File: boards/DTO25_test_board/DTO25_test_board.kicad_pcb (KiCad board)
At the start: 2 copper layers, 55.2 x 57.8 mm, 9 parts, among them J1 MicroFit_11, J2 Ultrafit_4, J3 Ultrafit_2, J4 Ultrafit_4

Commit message: DTO@% test board MKII
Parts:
- removed J1: MicroFit_11, footprints:Molex_MicroFit_3.0-11x3.00mm_Angled
- removed J2, J4: Ultrafit_4, footprints:Ultrafit_4
- removed J3: Ultrafit_2, footprints:Ultrafit_2
- added P1: CONN_02X03, footprints:Pin_Header_Straight_2x03, F.Cu at (154.3, 108.6)
- added P2: CONN_02X03, footprints:Pin_Header_Straight_2x03, F.Cu at (188.0, 109.9)
- added R6: DTO25, footprints:DTO25, F.Cu at (202.6, 92.1)
- moved R5 75.4 mm to (191.1, 132.7)
- moved R4 61.7 mm to (179.7, 92.1), turned to 0 degrees
- moved R3 28.2 mm to (145.4, 92.1), turned to 0 degrees
- moved R2 27.1 mm to (156.8, 92.1), turned to 0 degrees
- moved R1 25.7 mm to (168.3, 92.1), turned to 0 degrees
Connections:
- R1 pad 1: /Thermal_Plane -> /ThermalPlane1
- R2 pad 1: /Thermal_Plane -> /ThermalPlane2
- R3 pad 1: /Thermal_Plane -> /ThermalPlane3
- R4 pad 1: /Thermal_Plane -> /ThermalPlane4
- R5 pad 1: /Thermal_Plane -> /ThermalPlane5
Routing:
- net Net-(P1-Pad6): track 125.4 -> 8.98 mm, vias 1 -> 0
- net /Thermal_Plane: track 111.5 -> 0.00 mm, vias 22 -> 0
- net Net-(P1-Pad5): track 125.8 -> 15.1 mm, vias 1 -> 0
- net Net-(P1-Pad2): track 108.1 -> 8.98 mm
- net Net-(P1-Pad1): track 106.7 -> 16.6 mm
- net Net-(P1-Pad4): track 79.7 -> 7.40 mm, vias 1 -> 0
- net Net-(P2-Pad6): track 0.00 -> 47.0 mm
- net Net-(P2-Pad3): track 48.6 -> 15.0 mm
- net /ThermalPlane1: track 0.00 -> 24.5 mm, vias 0 -> 9
- net Net-(P2-Pad1): track 37.7 -> 13.3 mm
- net Net-(P1-Pad3): track 82.4 -> 66.2 mm, vias 1 -> 0
- net Net-(P2-Pad5): track 0.00 -> 14.5 mm
- net Net-(P2-Pad2): track 33.4 -> 45.2 mm
- net Net-(P2-Pad4): track 81.9 -> 80.1 mm
- net /ThermalPlane5: vias 0 -> 1
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- added copper zone on B.Cu, net /ThermalPlane1
- added copper zone on B.Cu, net /ThermalPlane2
- added copper zone on B.Cu, net /ThermalPlane3
- added copper zone on B.Cu, net /ThermalPlane4
- added copper zone on B.Cu, net /ThermalPlane5
- removed copper zone on B.Cu, net /Thermal_Plane
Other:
- board outline removed

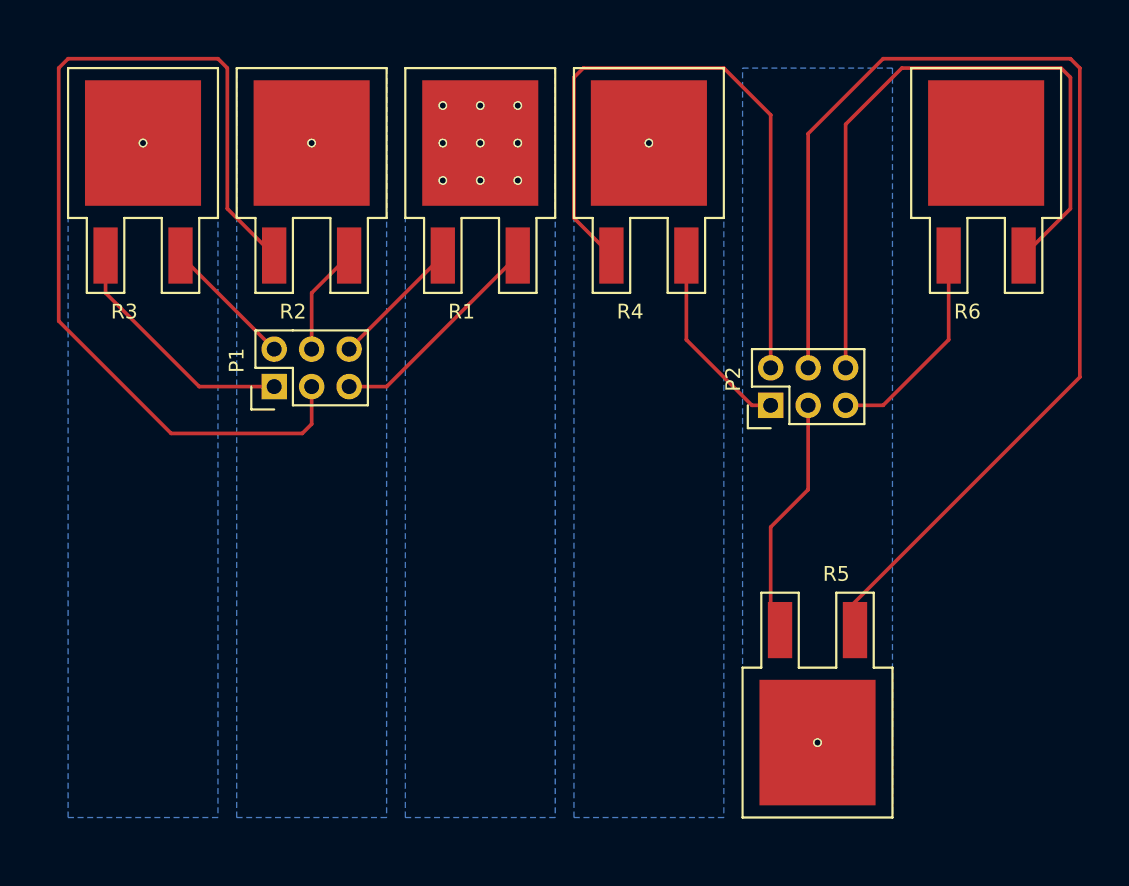
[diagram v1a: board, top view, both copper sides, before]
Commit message: Completed new DTO25 test board
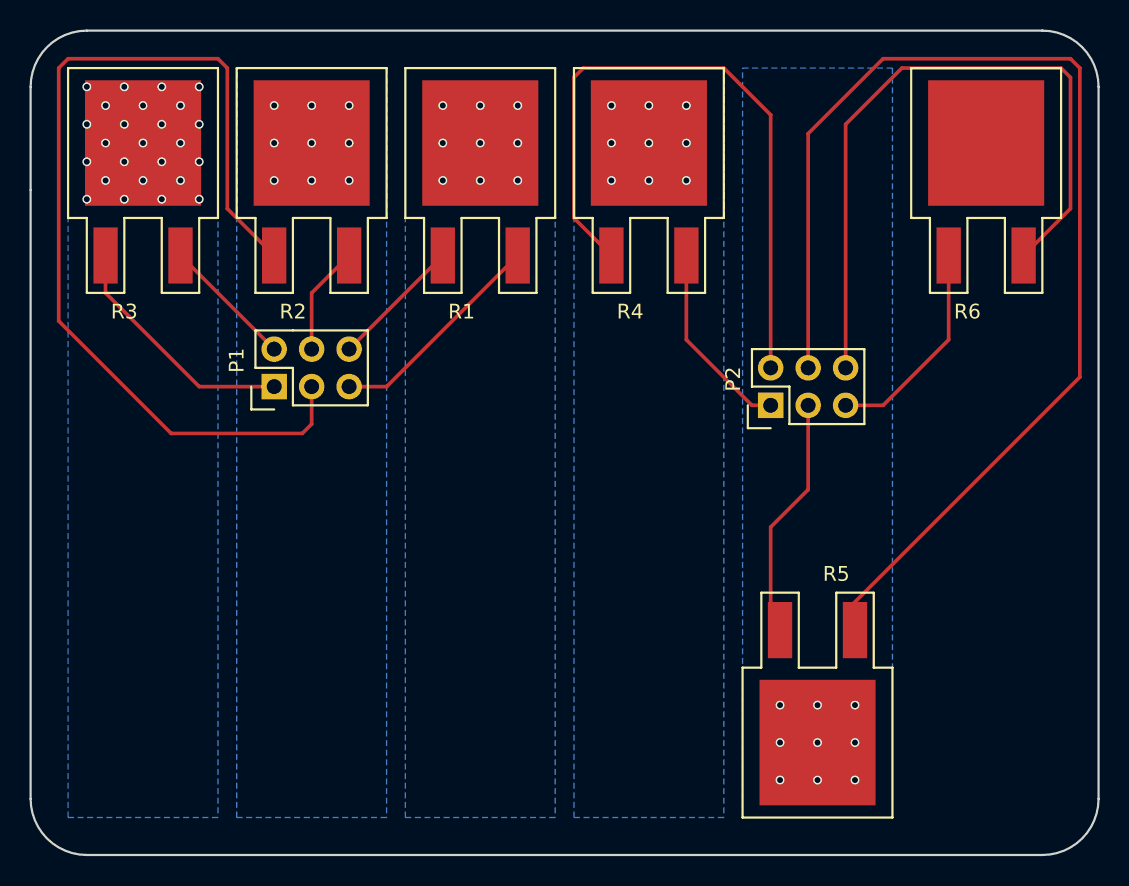
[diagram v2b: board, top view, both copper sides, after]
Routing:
- net /ThermalPlane3: track 0.00 -> 88.0 mm, vias 1 -> 25
- net /ThermalPlane4: track 0.00 -> 24.5 mm, vias 1 -> 9
- net /ThermalPlane5: track 0.00 -> 24.5 mm, vias 1 -> 9
- net /ThermalPlane2: track 0.00 -> 24.5 mm, vias 1 -> 9
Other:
- board outline added: 72.4 x 55.9 mm
